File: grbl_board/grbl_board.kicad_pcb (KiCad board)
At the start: 4 copper layers, 138.4 x 138.3 mm, 240 parts, among them J1 COOL, J10 DOOR, J11 PROBE, J12 INP, J13 LIM, J14 24V_VFD, J15 Spindle, J16 freq, J17 USB_B, J18 ICSP, J2 12VDC, J3 USB_B, J4 ICSP, J5 Screw_Terminal_01x04, J6 X_STEPPER, J7 Y_STEPPER, J8 Z_STEPPER, J9 E_STEPPER, Q1 BSS127S, Q2 BSS127S, Q3 ZVN4306GTA, Q4 IRF9Z24SPBF, Q5 BSS127S, Q6 BSS127S, Q7 BSS127S, SW1 SW_Push, SW2 SW_Push, U1 FT231XS, U10 6N137, U11 6N137, U12 6N137, U13 6N137, U14 6N137, U15 6N137, U16 6N137, U17 6N137, U18 6N137, U19 6N137, U2 ATmega2560-16AU, U20 6N137, U21 BD9G341EFJ, U22 LMV358, U23 OPA2192, U24 L7805, U25 FT231XS, U26 40106, U27 74LS155, U28 ATmega328P-AU, U29 74LS153, U3 LT1962-5, U30 74LS153, U4 BD9G341EFJ, U5 TMC5160_SILENTSTEPSTICK, U6 TMC5160_SILENTSTEPSTICK, U7 TMC5160_SILENTSTEPSTICK, U8 TMC5160_SILENTSTEPSTICK, U9 6N137, Y1 16M, Y2 16M

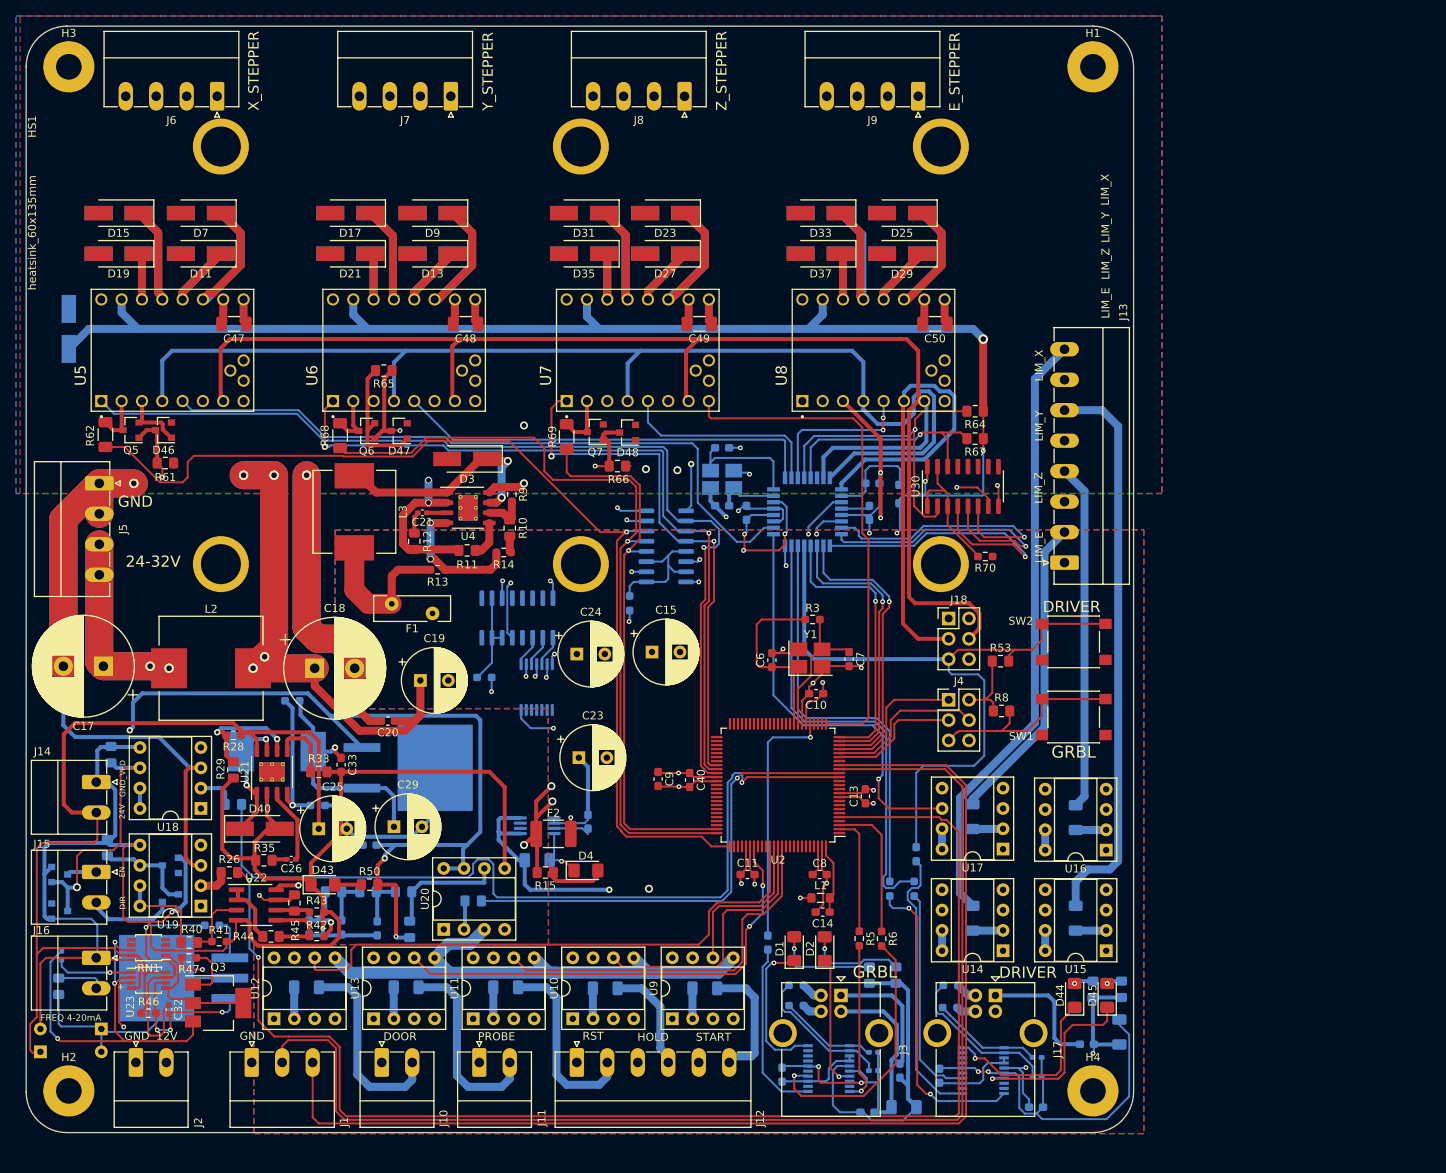
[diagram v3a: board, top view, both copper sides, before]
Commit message: added some descriptions in the schematic and added gerber file
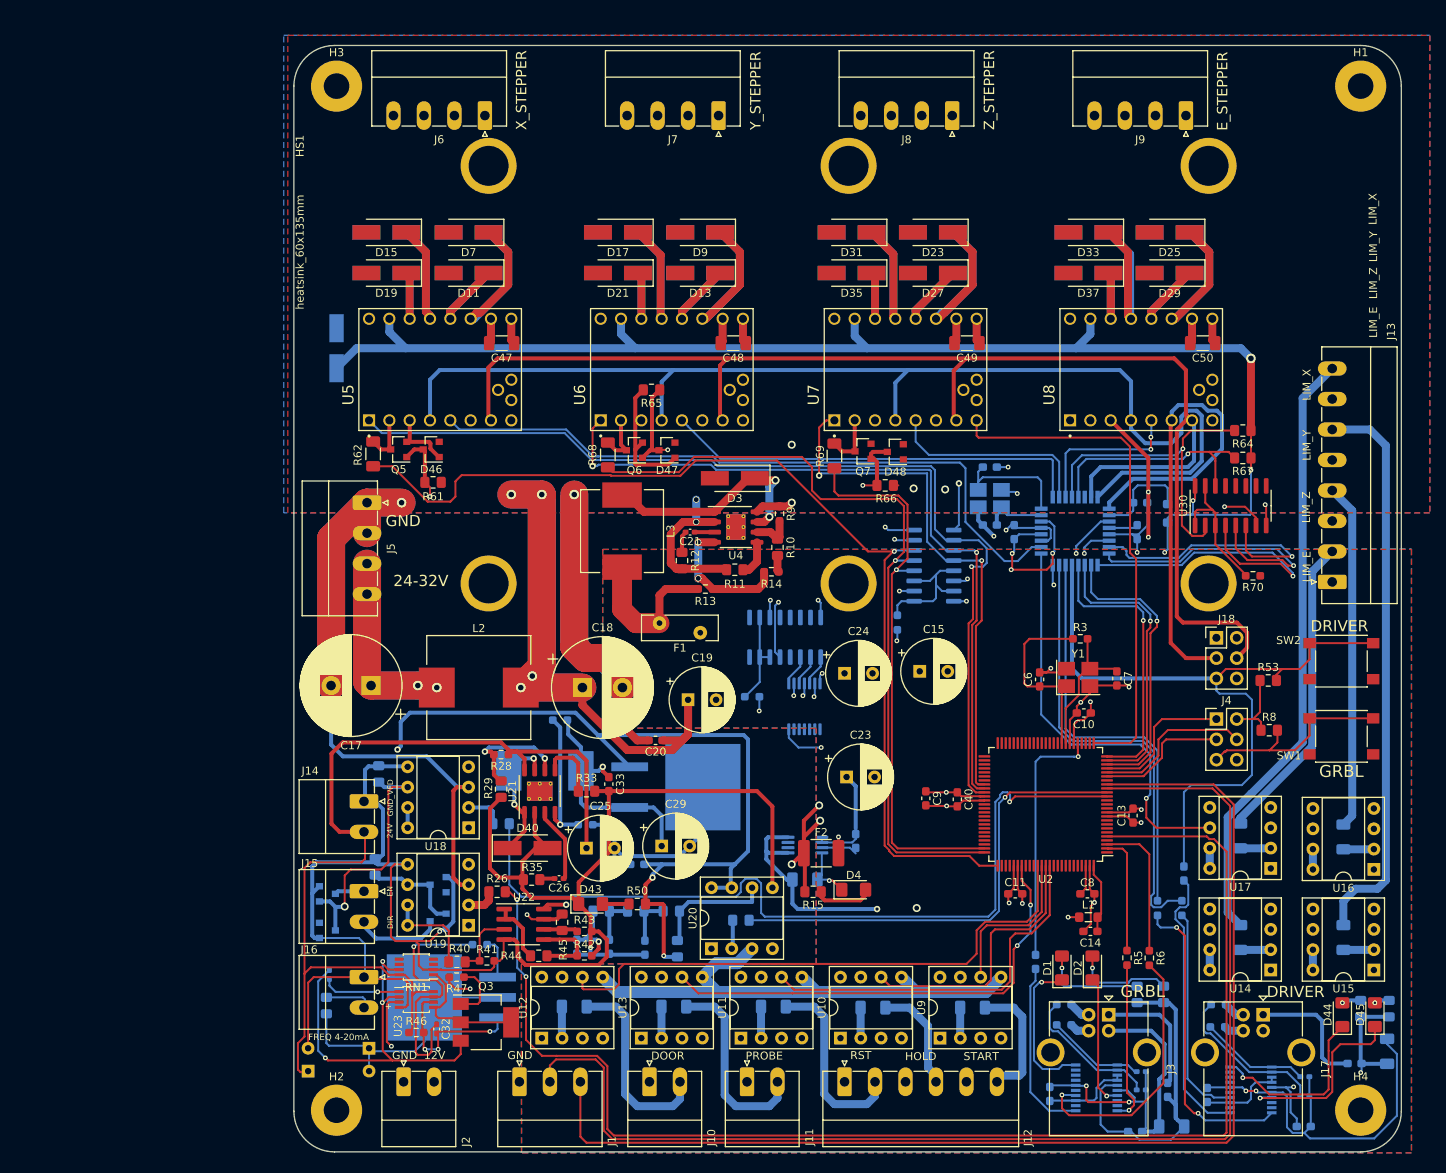
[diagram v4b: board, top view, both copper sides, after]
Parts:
- moved C14 33.6 mm to (172.4, 133.5)
- moved H4 33.6 mm to (206.2, 155.8)
- moved L1 33.6 mm to (172.1, 131.7)
- moved R1 33.6 mm to (169.1, 145.2)
- moved R18 33.6 mm to (132.8, 142.9)
- moved R2 33.6 mm to (169.1, 142.6)
- moved R52 33.6 mm to (188.4, 142.6)
- moved R55 33.6 mm to (180.8, 130.6)
- moved R56 33.6 mm to (183.8, 130.6)
- moved R7 33.6 mm to (181.5, 141.4)
- moved U10 33.6 mm to (141.2, 146.8)
- moved U2 33.6 mm to (166.8, 117.6)
- moved U29 33.6 mm to (152.8, 87.8)
- moved U9 33.6 mm to (153.6, 146.8)
- moved Y1 33.6 mm to (170.9, 101.7)
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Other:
- outline, holes or cut-outs redrawn

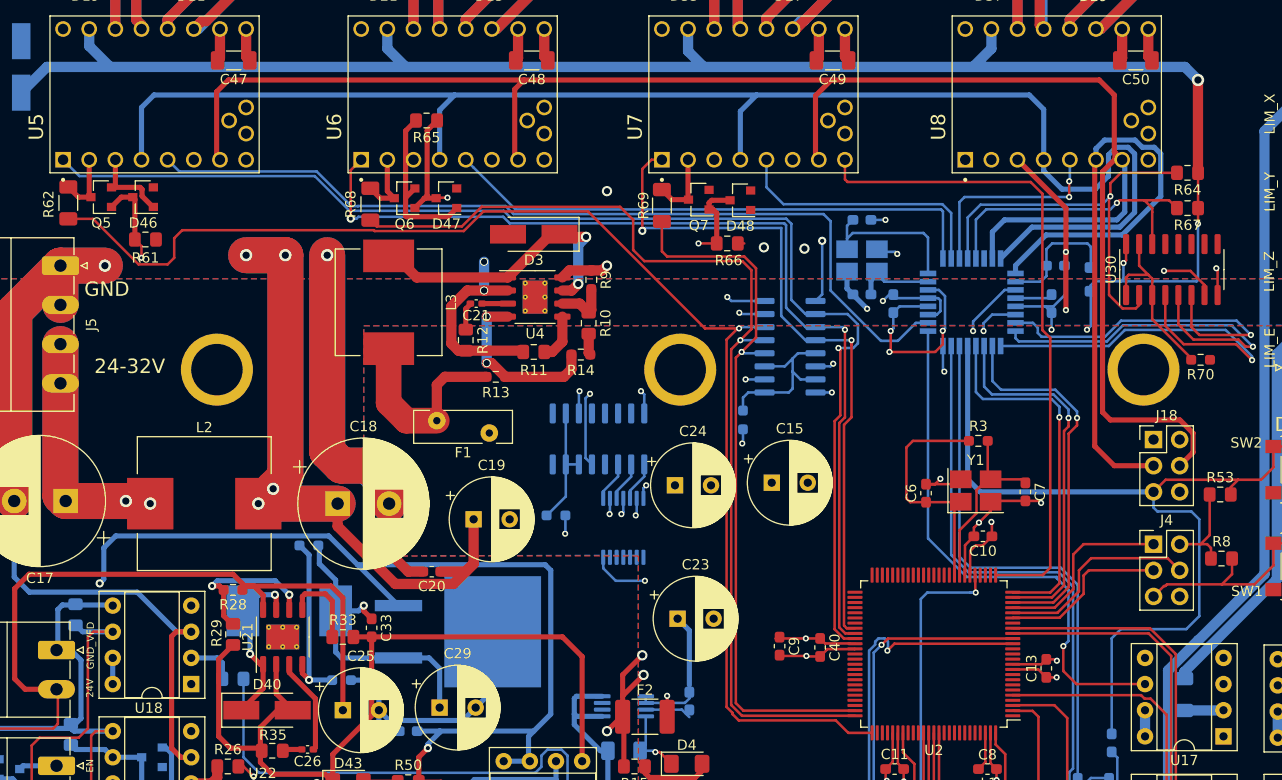
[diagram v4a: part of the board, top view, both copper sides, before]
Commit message: fixed limit switch disconnect issue
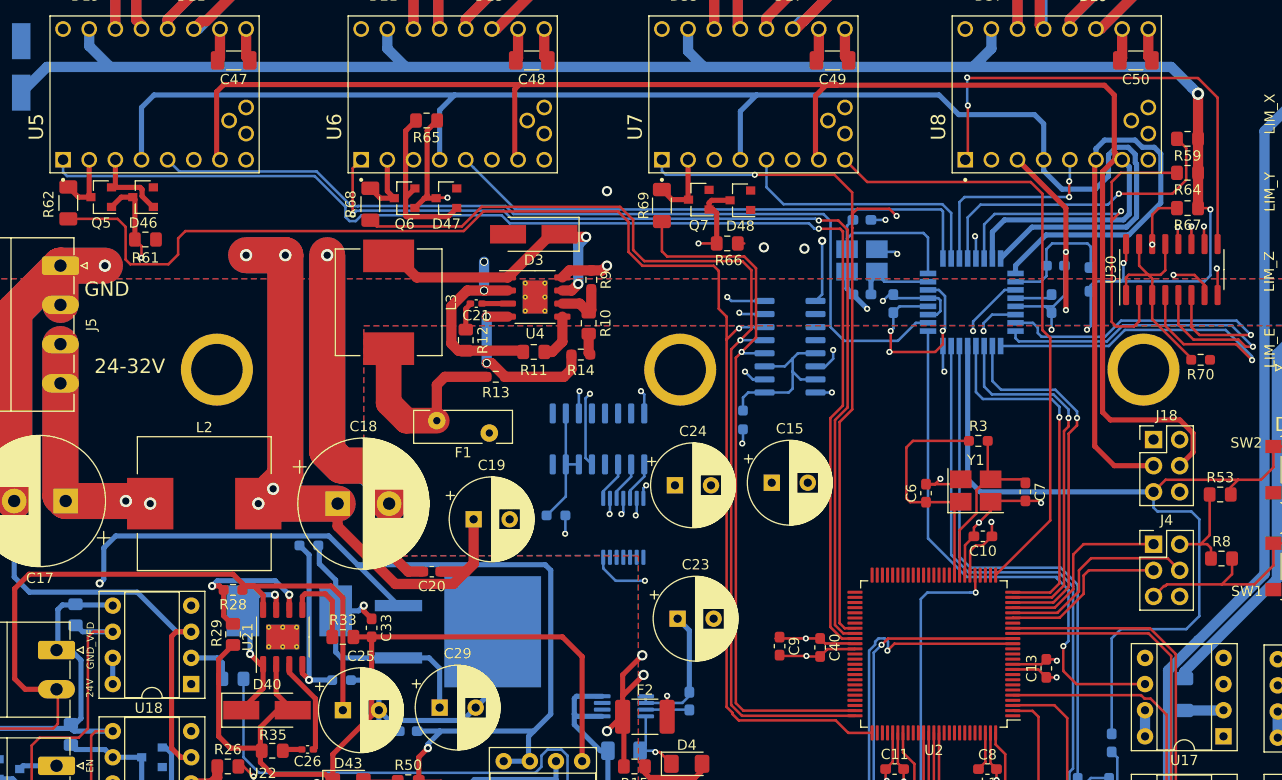
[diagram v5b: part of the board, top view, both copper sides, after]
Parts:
- added R59: 10k, Resistor_SMD:R_0805_2012Metric_Pad1.15x1.40mm_HandSolder, F.Cu at (191.5, 67.6)
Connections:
- net /spinlde_cntrl/12V renamed /spindle_cntrl/12V
- net /spinlde_cntrl/1V_REF renamed /spindle_cntrl/1V_REF
- net /spinlde_cntrl/24V_VFD renamed /spindle_cntrl/24V_VFD
- net /spinlde_cntrl/5V renamed /spindle_cntrl/5V
- net /spinlde_cntrl/GND_VFD renamed /spindle_cntrl/GND_VFD
- R64 pad 2: /aux_mcu/SEL1 -> /aux_mcu/SEL_E
- U28 pad 14: Net-(U28-Pad14) -> /aux_mcu/SEL_E
- U29 pad 10: /grbl_controller/DIR_X -> Net-(U29-Pad10)
- U29 pad 11: /grbl_controller/DIR_Y -> Net-(U29-Pad11)
- U29 pad 12: /grbl_controller/DIR_Z -> Net-(U29-Pad12)
- U29 pad 9: /stepper_drivers/E_DIR -> Net-(U29-Pad9)
- U30 pad 10: Net-(U30-Pad10) -> /grbl_controller/DIR_X
- U30 pad 11: Net-(U30-Pad11) -> /grbl_controller/DIR_Y
- U30 pad 12: Net-(U30-Pad12) -> /grbl_controller/DIR_Z
- U30 pad 13: Net-(U30-Pad13) -> Net-(R70-Pad2)
- U30 pad 2: /aux_mcu/SEL1 -> /aux_mcu/SEL_E
- U30 pad 9: Net-(U30-Pad9) -> /stepper_drivers/E_DIR
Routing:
- net /stepper_drivers/E_DIR: track 23.3 -> 70.7 mm, vias 1 -> 3
- net /aux_mcu/SEL_E: track 0.00 -> 44.5 mm, vias 0 -> 1
- net /grbl_controller/DIR_Y: track 94.4 -> 136.0 mm, vias 2 -> 3
- net /grbl_controller/DIR_X: track 122.4 -> 163.6 mm, vias 1 -> 2
- net /grbl_controller/DIR_Z: track 67.4 -> 100.1 mm, vias 2 -> 3
- net /aux_mcu/SEL0: track 73.2 -> 52.4 mm, vias 2 -> 3
- net /aux_mcu/SEL1: track 95.1 -> 85.7 mm
- net /grbl_controller/STEP_X: track 130.1 -> 136.1 mm
- net /aux_mcu/LIM_0: track 37.9 -> 33.1 mm
- net Net-(R70-Pad2): track 17.3 -> 21.7 mm
- net /CS_X: track 85.8 -> 87.9 mm
- net /stepper_drivers/EN: track 155.9 -> 154.1 mm
- net +5V: track 260.8 -> 262.1 mm

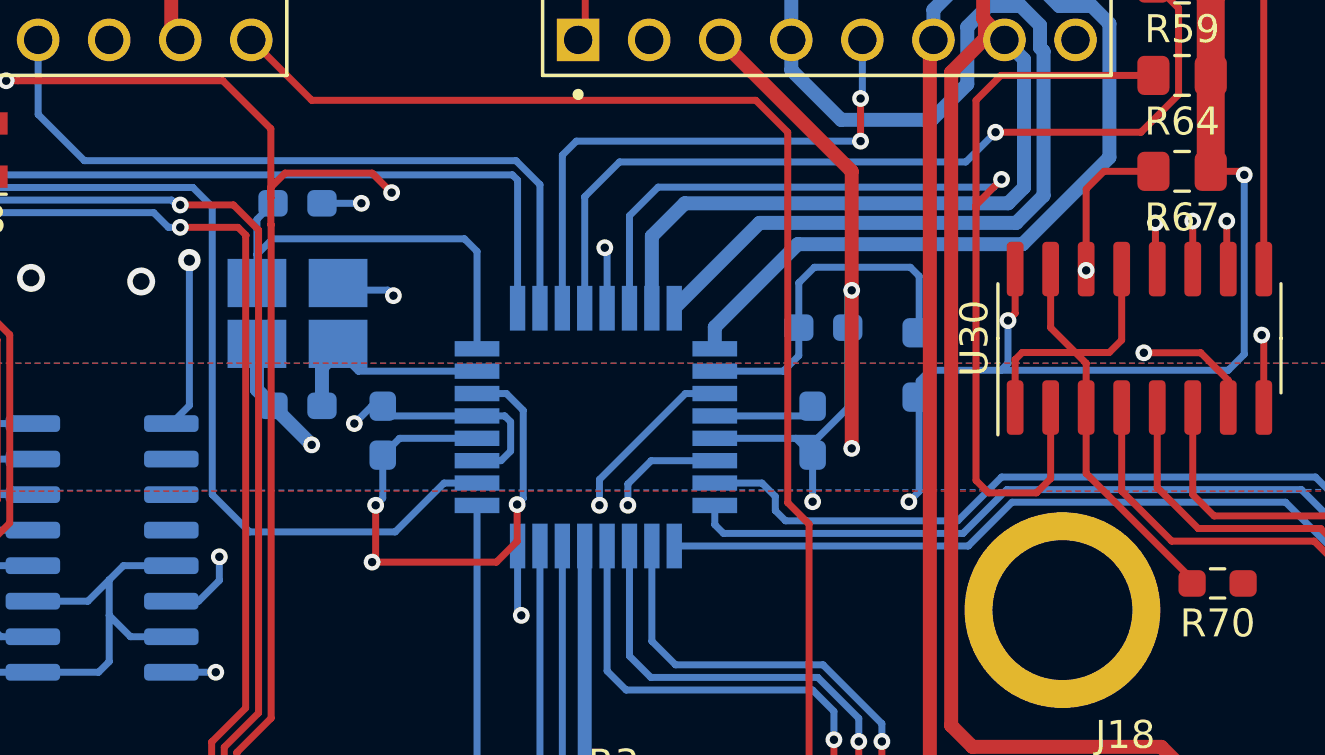
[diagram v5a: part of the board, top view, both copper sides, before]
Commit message: fixed copper fill
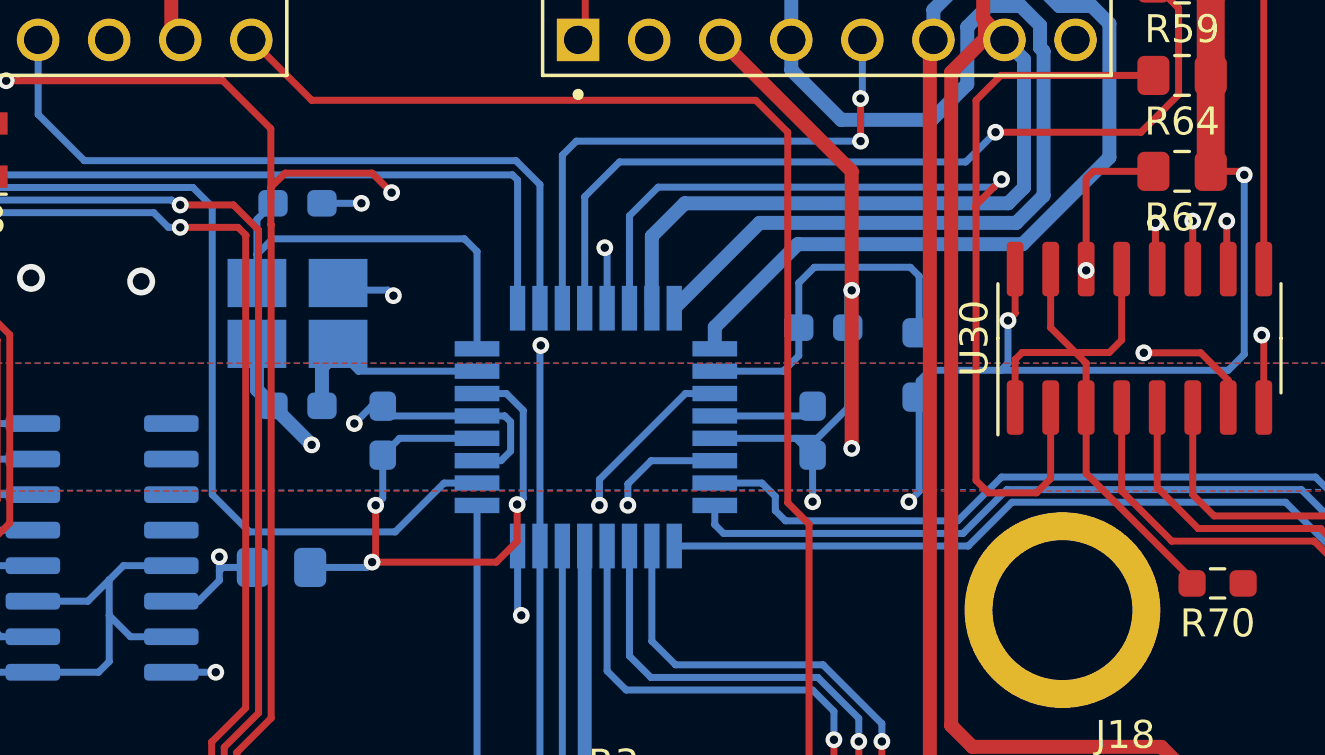
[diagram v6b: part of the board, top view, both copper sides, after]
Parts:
- added R60: 10k, Resistor_SMD:R_0805_2012Metric_Pad1.15x1.40mm_HandSolder, B.Cu at (159.3, 88.5)
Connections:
- net /aux_mcu/SEL_E renamed /aux_mcu/SEL_E1
- R56 pad 1: /aux_mcu/TX0 -> /aux_mcu/SEL_E0
- R67 pad 2: /aux_mcu/SEL0 -> /aux_mcu/SEL_E0
- U28 pad 31: /aux_mcu/TX0 -> /aux_mcu/SEL_E0
- U30 pad 14: /aux_mcu/SEL0 -> /aux_mcu/SEL_E0
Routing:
- net /aux_mcu/SEL_E0: track 0.00 -> 95.0 mm, vias 0 -> 2
- net /aux_mcu/TX0: track 56.9 -> 0.00 mm
- net /stepper_drivers/E_DIR: track 70.7 -> 47.5 mm, vias 3 -> 2
- net /aux_mcu/SEL0: track 52.4 -> 30.6 mm, vias 3 -> 2
- net +5V: track 262.1 -> 264.4 mm
